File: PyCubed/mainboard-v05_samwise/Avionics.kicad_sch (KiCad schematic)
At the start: 29 parts, among them SW1 KMR231NG LFS, U1 MAX706RESA, U2 ATSAMD51J20A-AU, Y1 32.768kHz

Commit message: made some changes to mainboard
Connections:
- net RPi_Rx renamed RPI_RX
- net RPi_Tx renamed RPI_TX
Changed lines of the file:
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@@
     )
   )
-  (global_label "RPi_Rx" (shape bidirectional) (at 90.17 118.11 180) (fields_autoplaced)
+  (global_label "RPI_RX" (shape bidirectional) (at 90.17 118.11 180) (fields_autoplaced)
     (effects (font (size 1.27 1.27)) (justify right))
-    (property "Intersheetrefs" "${INTERSHEET_REFS}" (at 80.476 118.11 0)
+    (property "Intersheetrefs" "${INTERSHEET_REFS}" (at 80.2946 118.11 0)
       (effects (font (size 1.27 1.27)) (justify right) hide)
     )
@@
     )
   )
-  (global_label "RPi_Tx" (shape bidirectional) (at 90.17 115.57 180) (fields_autoplaced)
+  (global_label "RPI_TX" (shape bidirectional) (at 90.17 115.57 180) (fields_autoplaced)
     (effects (font (size 1.27 1.27)) (justify right))
-    (property "Intersheetrefs" "${INTERSHEET_REFS}" (at 80.7784 115.57 0)
+    (property "Intersheetrefs" "${INTERSHEET_REFS}" (at 80.597 115.57 0)
       (effects (font (size 1.27 1.27)) (justify right) hide)
     )

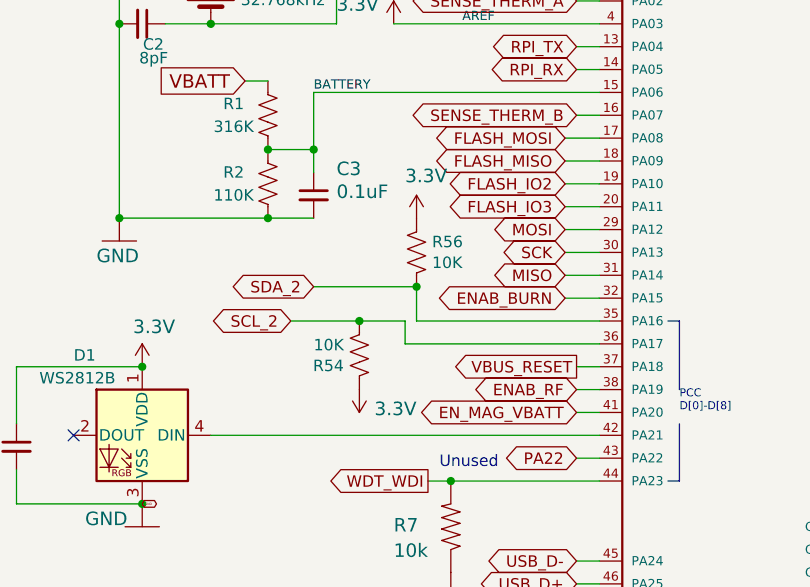
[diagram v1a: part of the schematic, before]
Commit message: cleanup
Removed traces to nothing
put connectors in spots that might work. Needs checking and connections
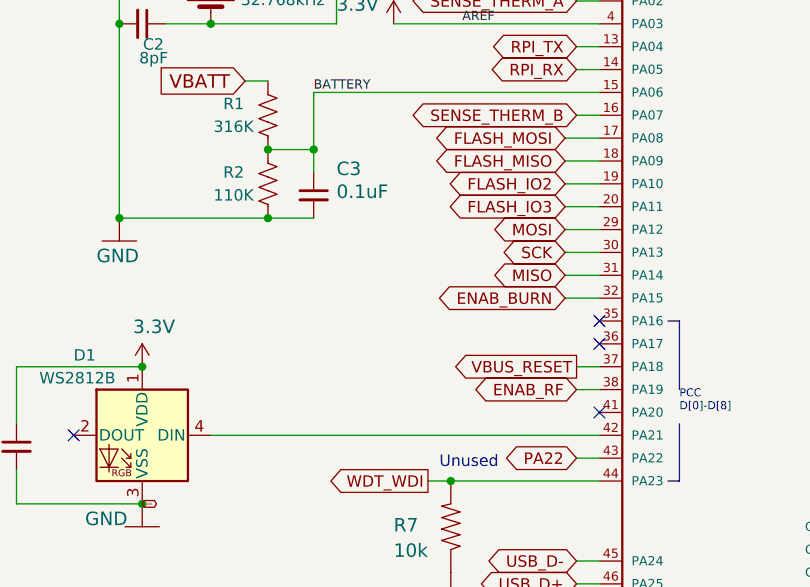
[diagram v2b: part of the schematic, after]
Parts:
- removed R54, R56: 10K, Resistor_SMD:R_0603_1608Metric, symbol Device:R_US
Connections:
- net EN_MAG_VBATT: no longer names the net of U2.41 (PA20)
- net SCL_2: no longer names the net of U2.36 (PA17)
- net SDA_2: no longer names the net of U2.35 (PA16)
- no-connect marks 2 -> 5
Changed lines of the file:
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@@
   (junction (at 124.46 173.99) (diameter 0) (color 0 0 0 0)
   )
-  (junction (at 66.04 146.05) (diameter 0) (color 0 0 0 0)
-  )
   (junction (at 78.74 77.47) (diameter 0) (color 0 0 0 0)
   )
@@
   (junction (at 125.73 92.71) (diameter 0) (color 0 0 0 0)
   )
-  (junction (at 72.39 142.24) (diameter 0) (color 0 0 0 0)
-  )
   (junction (at 39.37 113.03) (diameter 0) (color 0 0 0 0)
   )
@@
   (junction (at 137.16 85.09) (diameter 0) (color 0 0 0 0)
   )
+  (no_connect (at 92.71 156.21))
+  (no_connect (at 92.71 148.59))
   (no_connect (at 64.77 43.18))
   (no_connect (at 34.29 158.75))
+  (no_connect (at 92.71 146.05))
   (wire (pts (xy 123.19 153.67) (xy 127 153.67))
     (stroke (width 0) (type default))
@@
     (stroke (width 0) (type default))
   )
-  (wire (pts (xy 72.39 142.24) (xy 60.96 142.24))
-    (stroke (width 0) (type default))
-  )
   (wire (pts (xy 133.35 97.79) (xy 133.35 100.33))
     (stroke (width 0) (type default))
@@
     (stroke (width 0) (type default))
   )
-  (wire (pts (xy 71.12 146.05) (xy 66.04 146.05))
-    (stroke (width 0) (type default))
-  )
   (wire (pts (xy 123.19 90.17) (xy 125.73 90.17))
     (stroke (width 0) (type default))
@@
     (stroke (width 0) (type default))
   )
-  (wire (pts (xy 66.04 146.05) (xy 58.42 146.05))
-    (stroke (width 0) (type default))
-  )
   (wire (pts (xy 76.2 77.47) (xy 78.74 77.47))
     (stroke (width 0) (type default))
@@
     (stroke (width 0) (type default))
   )
-  (wire (pts (xy 92.71 146.05) (xy 72.39 146.05))
-    (stroke (width 0) (type default))
-  )
   (wire (pts (xy 115.57 38.1) (xy 100.33 38.1))
     (stroke (width 0) (type default))
@@
     (stroke (width 0) (type default))
   )
-  (wire (pts (xy 72.39 146.05) (xy 72.39 142.24))
-    (stroke (width 0) (type default))
-  )
   (wire (pts (xy 123.19 156.21) (xy 127 156.21))
     (stroke (width 0) (type default))
@@
     (stroke (width 0) (type default))
   )
-  (wire (pts (xy 71.12 148.59) (xy 71.12 146.05))
-    (stroke (width 0) (type default))
-  )
   (wire (pts (xy 124.46 173.99) (xy 124.46 176.53))
     (stroke (width 0) (type default))
@@
     (stroke (width 0) (type default))
   )
-  (wire (pts (xy 92.71 148.59) (xy 71.12 148.59))
-    (stroke (width 0) (type default))
-  )
   (wire (pts (xy 64.77 38.1) (xy 52.07 38.1))
     (stroke (width 0) (type default))
@@
   )
   (wire (pts (xy 133.35 95.25) (xy 137.16 95.25))
-    (stroke (width 0) (type default))
-  )
-  (wire (pts (xy 92.71 156.21) (xy 90.17 156.21))
     (stroke (width 0) (type default))
   )
@@
     )
   )
-  (global_label "SCL_2" (shape bidirectional) (at 58.42 146.05 180) (fields_autoplaced)
-    (effects (font (size 1.27 1.27)) (justify right))
-    (property "Intersheetrefs" "${INTERSHEET_REFS}" (at 49.5312 146.05 0)
-      (effects (font (size 1.27 1.27)) (justify right) hide)
-    )
-  )
   (global_label "SWCLK" (shape bidirectional) (at 85.09 90.17 180) (fields_autoplaced)
     (effects (font (size 1.27 1.27)) (justify right))
     (property "Intersheetrefs" "${INTERSHEET_REFS}" (at 75.6569 90.17 0)
-      (effects (font (size 1.27 1.27)) (justify right) hide)
-    )
-  )
-  (global_label "SDA_2" (shape bidirectional) (at 60.96 142.24 180) (fields_autoplaced)
-    (effects (font (size 1.27 1.27)) (justify right))
-    (property "Intersheetrefs" "${INTERSHEET_REFS}" (at 52.0107 142.24 0)
       (effects (font (size 1.27 1.27)) (justify right) hide)
     )
@@
     (property "Intersheetrefs" "${INTERSHEET_REFS}" (at 139.3965 135.89 0)
       (effects (font (size 1.27 1.27)) (justify left) hide)
-    )
-  )
-  (global_label "EN_MAG_VBATT" (shape bidirectional) (at 90.17 156.21 180) (fields_autoplaced)
-    (effects (font (size 1.27 1.27)) (justify right))
-    (property "Intersheetrefs" "${INTERSHEET_REFS}" (at 74.2387 156.1306 0)
-      (effects (font (size 1.27 1.27)) (justify right) hide)
     )
   )
@@
         )
       )
-    )
-  )
-  (symbol (lib_id "Device:R_US") (at 66.04 149.86 0) (mirror x) (unit 1)
-    (in_bom yes) (on_board yes) (dnp no)
-    (property "Reference" "R54" (at 64.3128 151.0284 0)
-      (effects (font (size 1.27 1.27)) (justify right))
-    )
-    (property "Value" "10K" (at 64.3128 148.717 0)
-      (effects (font (size 1.27 1.27)) (justify right))
-    )
-    (property "Footprint" "Resistor_SMD:R_0603_1608Metric" (at 67.056 149.606 90)
-      (effects (font (size 1.27 1.27)) hide)
-    )
-    (property "Datasheet" "" (at 66.04 149.86 0)
-      (effects (font (size 1.27 1.27)) hide)
-    )
-    (property "Description" "10K 0603" (at 64.3128 153.5684 0)
-      (effects (font (size 1.27 1.27)) hide)
-    )
-    (pin "1")
-    (pin "2")
-    (instances
-      (project "mainboard"
-        (path "/db20b18b-d25a-428e-8229-70a189e1de75/00000000-0000-0000-0000-00005cec5a72"
-          (reference "R54") (unit 1)
-        )
-      )
-    )
-  )
-  (symbol (lib_id "mainboard:3.3V") (at 66.04 153.67 180) (unit 1)
-    (in_bom yes) (on_board yes) (dnp no)
-    (property "Reference" "#SUPPLY0103" (at 66.04 153.67 0)
-      (effects (font (size 1.27 1.27)) hide)
-    )
-    (property "Value" "3.3V" (at 72.39 154.94 0)
-      (effects (font (size 1.4986 1.4986)) (justify left bottom))
-    )
-    (property "Footprint" "" (at 66.04 153.67 0)
-      (effects (font (size 1.27 1.27)) hide)
-    )
-    (property "Datasheet" "" (at 66.04 153.67 0)
-      (effects (font (size 1.27 1.27)) hide)
-    )
-    (pin "1")
-    (instances
-      (project "mainboard"
-        (path "/db20b18b-d25a-428e-8229-70a189e1de75/00000000-0000-0000-0000-00005cec5a72"
-          (reference "#SUPPLY0103") (unit 1)
-        )
-      )
-    )
-  )
-  (symbol (lib_id "Device:R_US") (at 72.39 138.43 0) (mirror y) (unit 1)
-    (in_bom yes) (on_board yes) (dnp no)
-    (property "Reference" "R56" (at 74.1172 137.2616 0)
-      (effects (font (size 1.27 1.27)) (justify right))
-    )
-    (property "Value" "10K" (at 74.1172 139.573 0)
-      (effects (font (size 1.27 1.27)) (justify right))
-    )
-    (property "Footprint" "Resistor_SMD:R_0603_1608Metric" (at 71.374 138.684 90)
-      (effects (font (size 1.27 1.27)) hide)
-    )
-    (property "Datasheet" "" (at 72.39 138.43 0)
-      (effects (font (size 1.27 1.27)) hide)
-    )
-    (property "Description" "10K 0603" (at 74.1172 134.7216 0)
-      (effects (font (size 1.27 1.27)) hide)
-    )
-    (pin "1")
-    (pin "2")
-    (instances
-      (project "mainboard"
-        (path "/db20b18b-d25a-428e-8229-70a189e1de75/00000000-0000-0000-0000-00005cec5a72"
-          (reference "R56") (unit 1)
-        )
-      )
-    )
-  )
-  (symbol (lib_id "mainboard:3.3V") (at 72.39 134.62 0) (unit 1)
-    (in_bom yes) (on_board yes) (dnp no)
-    (property "Reference" "#SUPPLY0105" (at 72.39 134.62 0)
-      (effects (font (size 1.27 1.27)) hide)
-    )
-    (property "Value" "3.3V" (at 71.12 130.81 0)
-      (effects (font (size 1.4986 1.4986)) (justify left bottom))
-    )
-    (property "Footprint" "" (at 72.39 134.62 0)
-      (effects (font (size 1.27 1.27)) hide)
-    )
-    (property "Datasheet" "" (at 72.39 134.62 0)
-      (effects (font (size 1.27 1.27)) hide)
-    )
-    (pin "1")
-    (instances
-      (project "mainboard"
-        (path "/db20b18b-d25a-428e-8229-70a189e1de75/00000000-0000-0000-0000-00005cec5a72"
-          (reference "#SUPPLY0105") (unit 1)
-        )
-      )

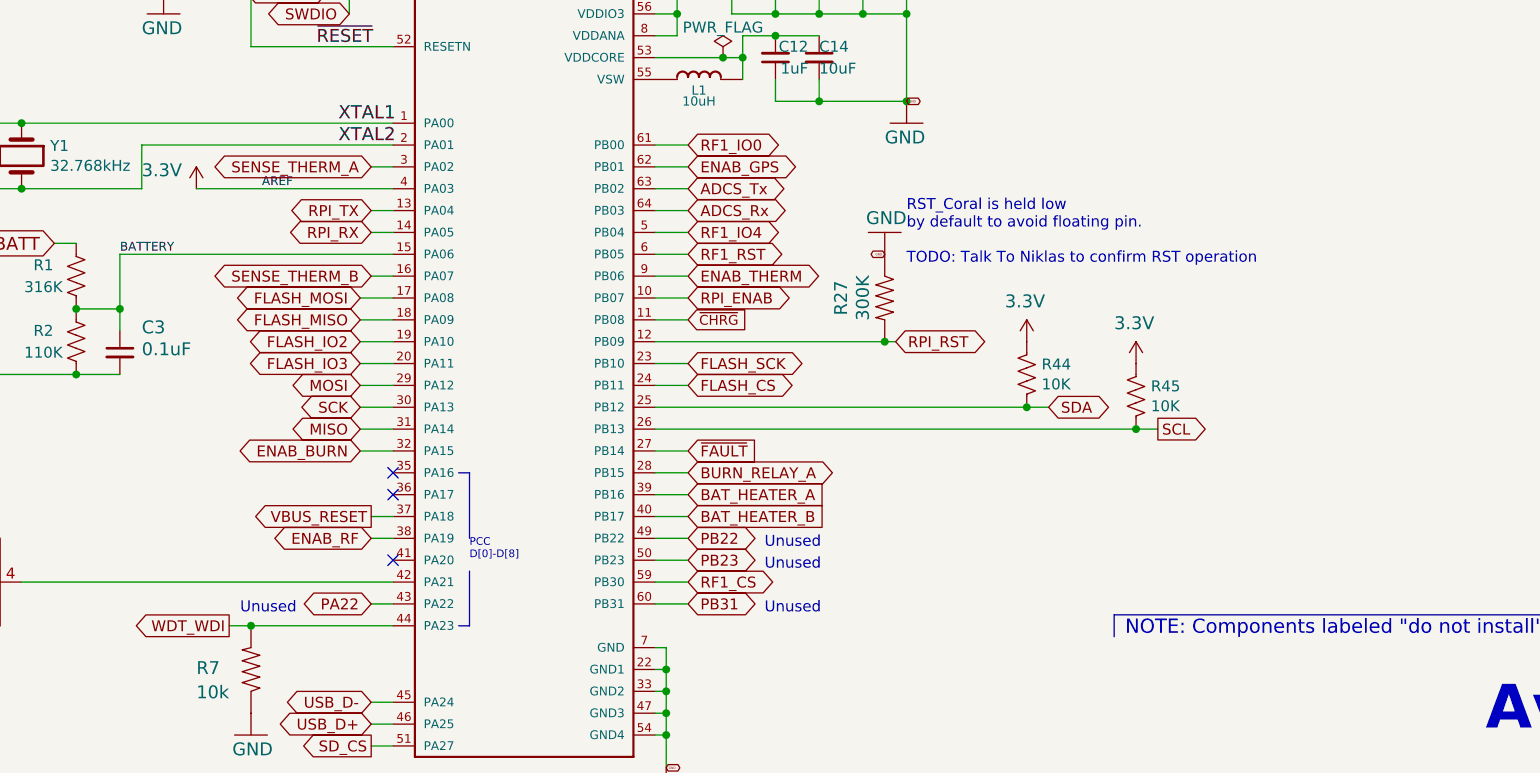
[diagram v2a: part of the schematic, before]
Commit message: a bit of schematic cleanup
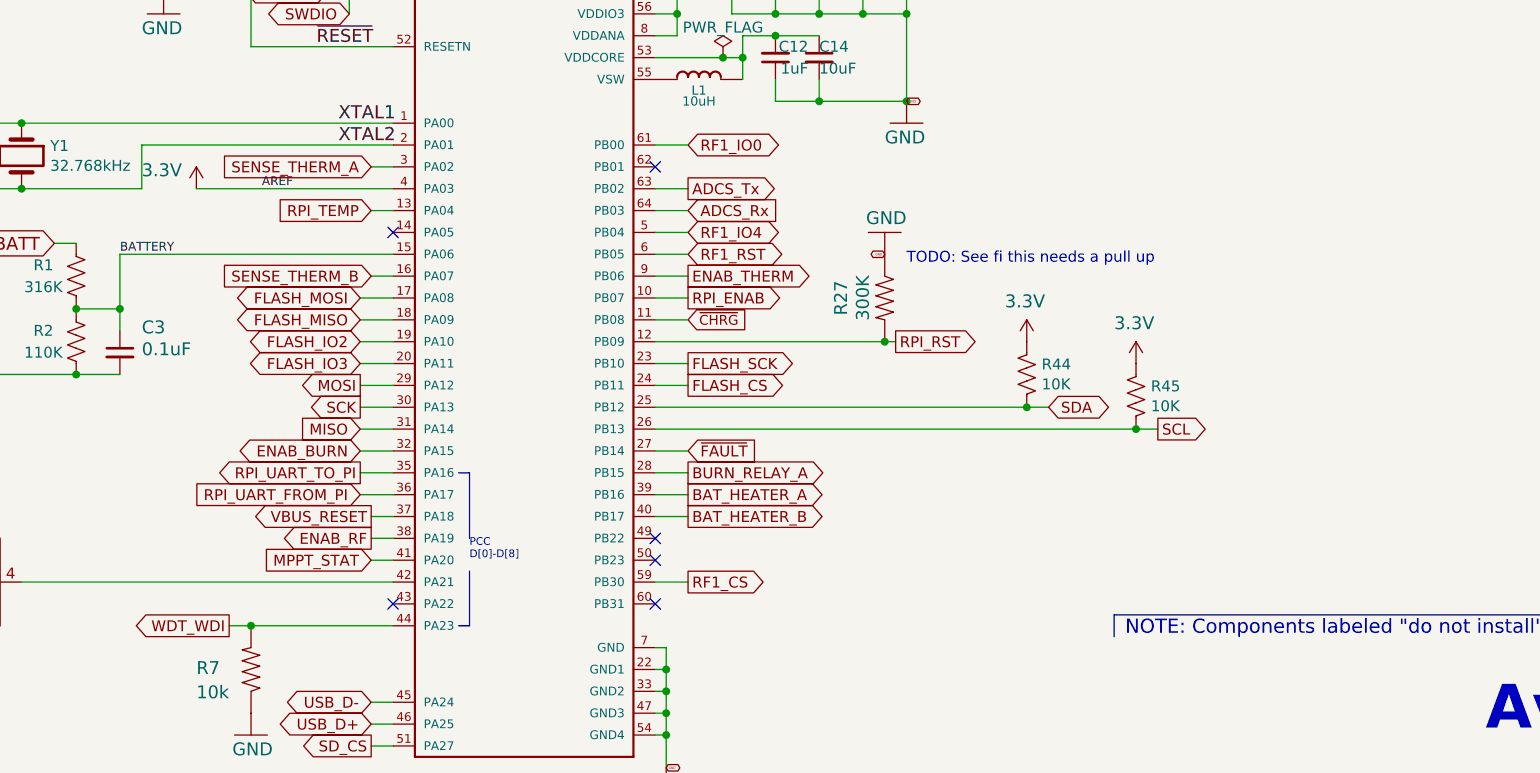
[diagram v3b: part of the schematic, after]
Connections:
- net RPI_UART_TO_PI: now reaches U2.35 (PA16)
- net RPI_UART_FROM_PI: now reaches U2.36 (PA17)
- net MPPT_STAT: now reaches U2.41 (PA20)
- net ENAB_GPS: no longer names the net of U2.62 (PB01)
- net PA22: no longer names the net of U2.43 (PA22)
- net PB22: no longer names the net of U2.49 (PB22)
- net PB23: no longer names the net of U2.50 (PB23)
- net PB31: no longer names the net of U2.60 (PB31)
- net RPI_RX: no longer names the net of U2.14 (PA05)
- net RPI_TX renamed RPI_TEMP
- no-connect marks 5 -> 8
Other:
- note added: "TODO: See fi this needs a pull up"
- note removed: "RST_Coral is held low by default to avoid floating pin. TODO: Talk To Niklas to confirm RST operation"
- note removed: "Unused"
